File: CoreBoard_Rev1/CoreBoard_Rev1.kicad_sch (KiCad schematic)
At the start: 87 parts, among them J1 RJ45_LED_Shielded, SW1 SW_Push, SW10 SW_Push, SW11 SW_Push, SW12 SW_Push, SW13 SW_Push, SW14 SW_Push, SW15 SW_Push, SW16 SW_SPDT, SW17 SW_SPDT, SW2 SW_Push, SW3 SW_Push, SW4 SW_Push, SW5 SW_Push, SW6 SW_Push, SW7 SW_Push, SW8 SW_Push, SW9 SW_Push, U1 Teensy4.1_DEV-16771, U2 TSR_1-2450, U3 TSR_1-2450, U4 74LS148, U5 74LS148, U6 74LS00

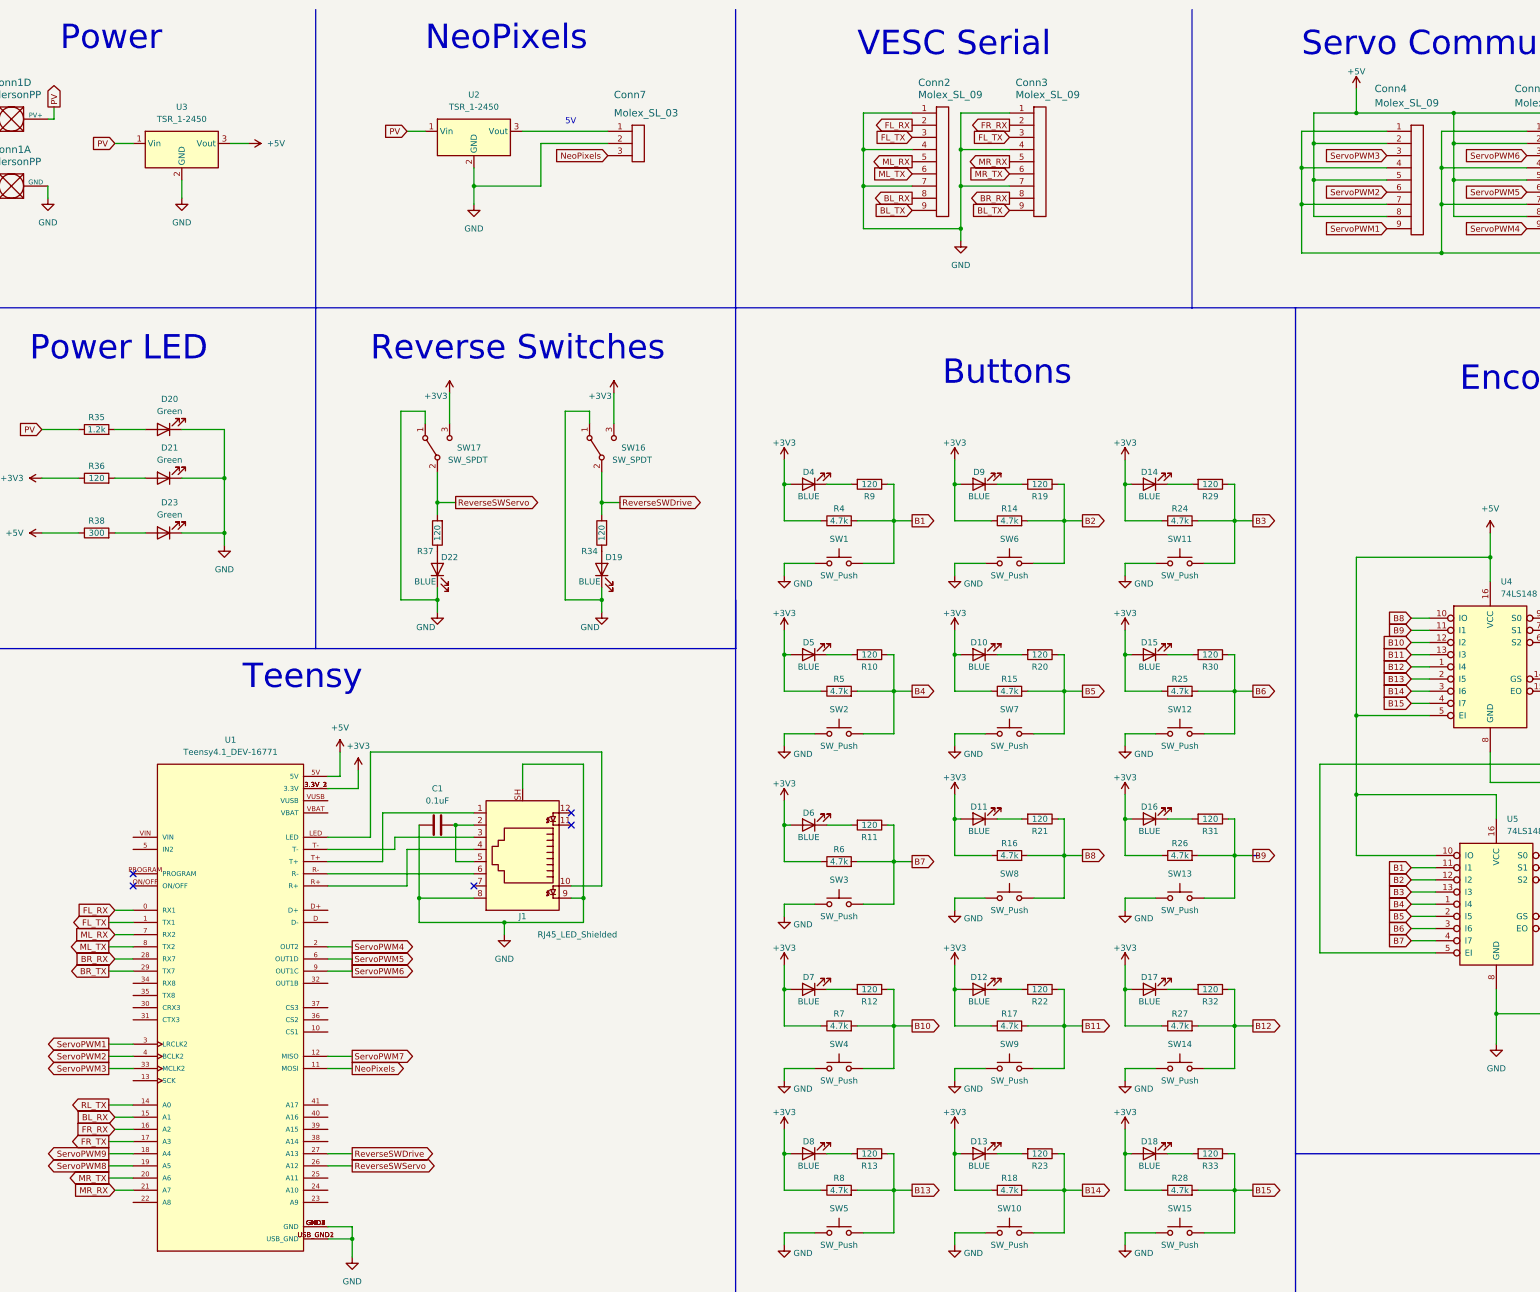
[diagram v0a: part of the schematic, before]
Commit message: Changes to LED Resistance value
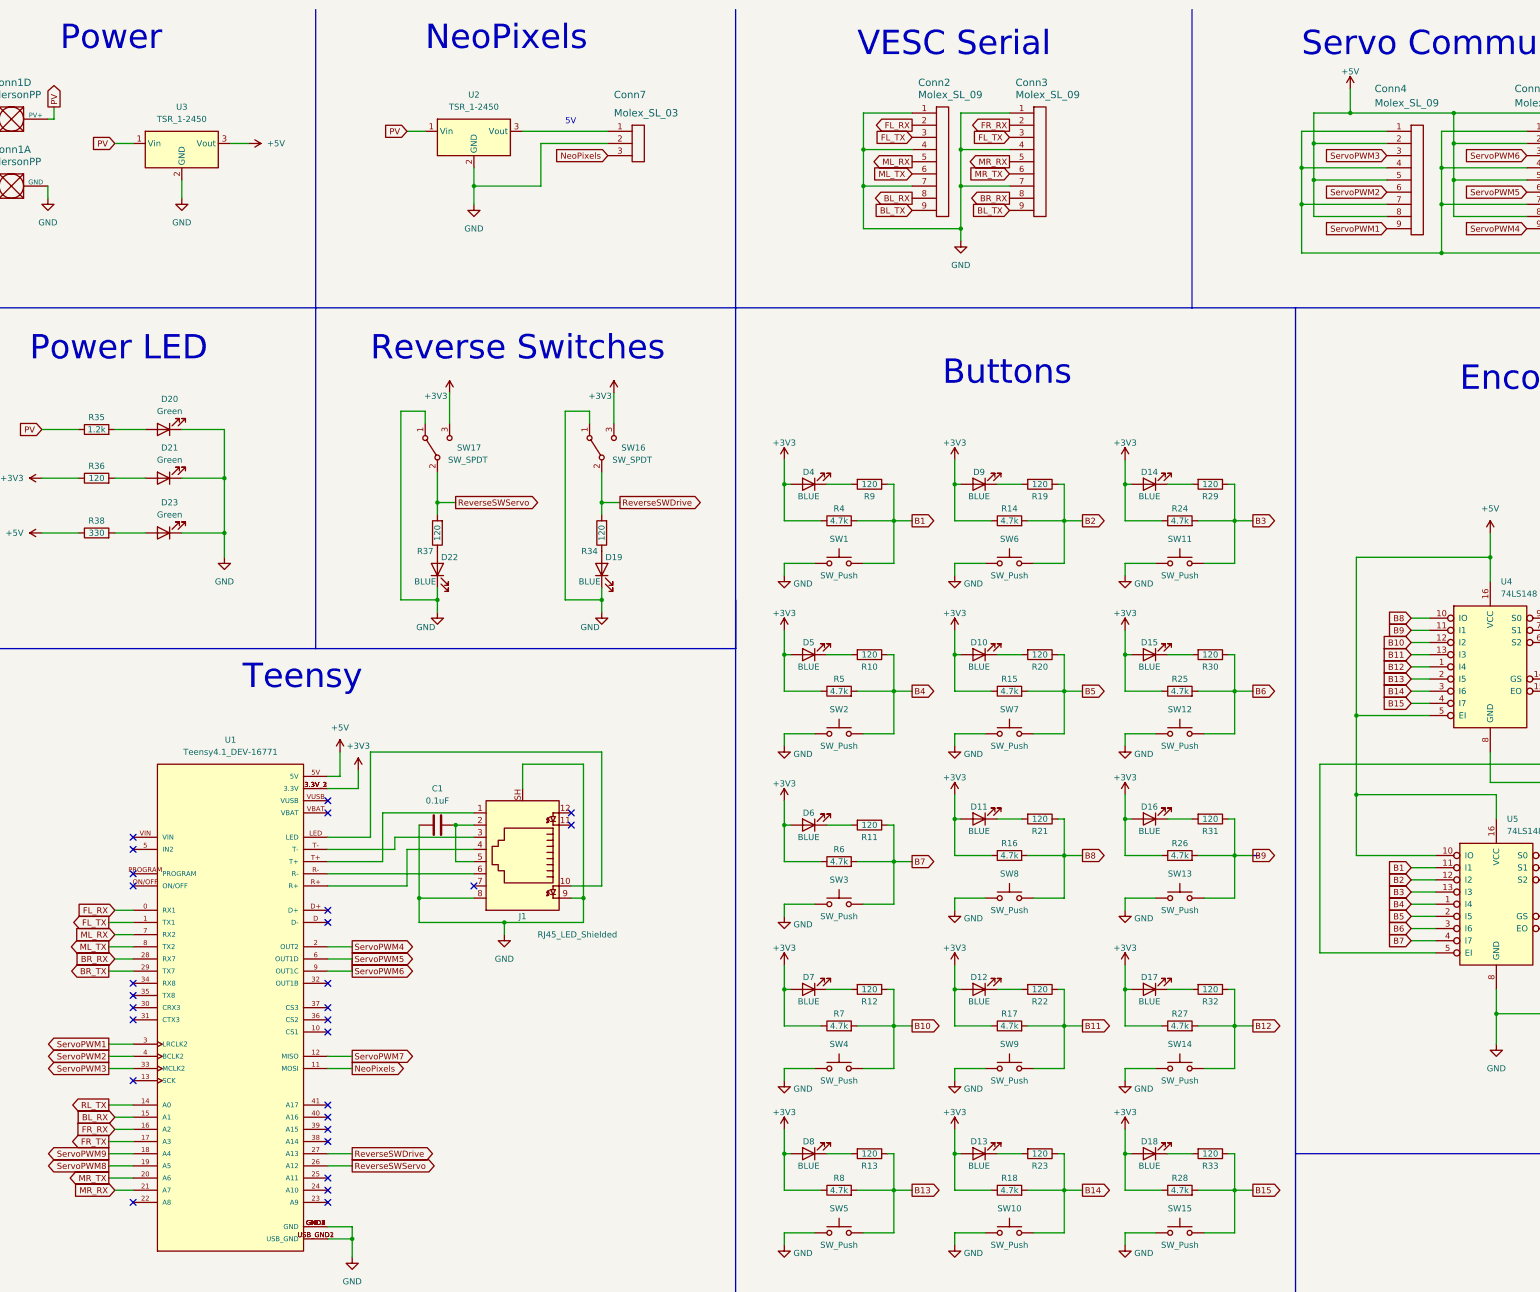
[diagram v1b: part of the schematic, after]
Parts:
- R38: value 300 -> 330
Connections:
- no-connect marks 8 -> 31
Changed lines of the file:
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@@
   (junction (at 326.39 63.5) (diameter 0) (color 0 0 0 0)
   )
-  (junction (at 308.61 34.29) (diameter 0) (color 0 0 0 0)
-  )
   (junction (at 212.09 190.5) (diameter 0) (color 0 0 0 0)
   )
@@
   (junction (at 113.03 198.12) (diameter 0) (color 0 0 0 0)
   )
+  (junction (at 307.34 34.29) (diameter 0) (color 0 0 0 0)
+  )
+  (no_connect (at 53.34 220.98))
+  (no_connect (at 93.98 220.98))
+  (no_connect (at 93.98 248.92))
+  (no_connect (at 93.98 246.38))
+  (no_connect (at 53.34 215.9))
+  (no_connect (at 93.98 177.8))
+  (no_connect (at 53.34 187.96))
+  (no_connect (at 93.98 223.52))
+  (no_connect (at 93.98 203.2))
   (no_connect (at 53.34 195.58))
   (no_connect (at 350.52 204.47))
+  (no_connect (at 93.98 215.9))
+  (no_connect (at 93.98 200.66))
+  (no_connect (at 53.34 218.44))
+  (no_connect (at 93.98 259.08))
   (no_connect (at 144.78 182.88))
+  (no_connect (at 53.34 261.62))
   (no_connect (at 53.34 193.04))
+  (no_connect (at 53.34 185.42))
+  (no_connect (at 93.98 226.06))
+  (no_connect (at 93.98 261.62))
   (no_connect (at 349.25 152.4))
   (no_connect (at 350.52 201.93))
   (no_connect (at 124.46 195.58))
+  (no_connect (at 53.34 223.52))
+  (no_connect (at 93.98 180.34))
+  (no_connect (at 53.34 236.22))
+  (no_connect (at 93.98 241.3))
+  (no_connect (at 93.98 243.84))
   (no_connect (at 144.78 180.34))
+  (no_connect (at 93.98 256.54))
   (wire (pts (xy 260.35 233.68) (xy 266.7 233.68))
     (stroke (width 0) (type default))
   )
+  (wire (pts (xy 307.34 34.29) (xy 328.93 34.29))
+    (stroke (width 0) (type default))
+  )
   (wire (pts (xy 260.35 251.46) (xy 260.35 259.08))
     (stroke (width 0) (type default))
@@
     (stroke (width 0) (type default))
   )
+  (wire (pts (xy 307.34 34.29) (xy 299.72 34.29))
+    (stroke (width 0) (type default))
+  )
   (wire (pts (xy 224.79 217.17) (xy 224.79 224.79))
     (stroke (width 0) (type default))
@@
     (stroke (width 0) (type default))
   )
-  (wire (pts (xy 102.87 167.64) (xy 102.87 185.42))
-    (stroke (width 0) (type default))
-  )
   (wire (pts (xy 48.26 241.3) (xy 53.34 241.3))
     (stroke (width 0) (type default))
@@
     (stroke (width 0) (type default))
   )
-  (wire (pts (xy 102.87 167.64) (xy 151.13 167.64))
-    (stroke (width 0) (type default))
-  )
   (wire (pts (xy 116.84 138.43) (xy 116.84 135.89))
     (stroke (width 0) (type default))
@@
     (stroke (width 0) (type default))
   )
-  (wire (pts (xy 299.72 34.29) (xy 308.61 34.29))
-    (stroke (width 0) (type default))
-  )
   (wire (pts (xy 260.35 270.51) (xy 260.35 267.97))
     (stroke (width 0) (type default))
@@
     (stroke (width 0) (type default))
   )
-  (wire (pts (xy 308.61 34.29) (xy 328.93 34.29))
-    (stroke (width 0) (type default))
-  )
   (wire (pts (xy 247.65 163.83) (xy 247.65 154.94))
     (stroke (width 0) (type default))
@@
     (stroke (width 0) (type default))
   )
-  (wire (pts (xy 72.39 121.92) (xy 72.39 124.46))
+  (wire (pts (xy 72.39 121.92) (xy 72.39 127))
     (stroke (width 0) (type default))
   )
@@
     (stroke (width 0) (type default))
   )
+  (wire (pts (xy 102.87 167.64) (xy 102.87 185.42))
+    (stroke (width 0) (type default))
+  )
+  (wire (pts (xy 151.13 167.64) (xy 102.87 167.64))
+    (stroke (width 0) (type default))
+  )
   (wire (pts (xy 247.65 259.08) (xy 251.46 259.08))
     (stroke (width 0) (type default))
@@
     (stroke (width 0) (type default))
   )
-  (wire (pts (xy 308.61 29.21) (xy 308.61 34.29))
+  (wire (pts (xy 307.34 29.21) (xy 307.34 34.29))
     (stroke (width 0) (type default))
   )
@@
       (effects (font (size 1.27 1.27)))
     )
-    (property "Value" "300" (at 45.72 121.92 90)
+    (property "Value" "330" (at 45.72 121.92 90)
       (effects (font (size 1.27 1.27)))
     )
@@
     )
   )
-  (symbol (lib_id "power:GND") (at 72.39 124.46 0) (unit 1)
+  (symbol (lib_id "power:GND") (at 72.39 127 0) (unit 1)
     (in_bom yes) (on_board yes) (dnp no) (fields_autoplaced)
-    (property "Reference" "#PWR047" (at 72.39 130.81 0)
+    (property "Reference" "#PWR047" (at 72.39 133.35 0)
       (effects (font (size 1.27 1.27)) hide)
     )
-    (property "Value" "GND" (at 72.39 129.54 0)
+    (property "Value" "GND" (at 72.39 132.08 0)
       (effects (font (size 1.27 1.27)))
     )
-    (property "Footprint" "" (at 72.39 124.46 0)
+    (property "Footprint" "" (at 72.39 127 0)
       (effects (font (size 1.27 1.27)) hide)
     )
-    (property "Datasheet" "" (at 72.39 124.46 0)
+    (property "Datasheet" "" (at 72.39 127 0)
       (effects (font (size 1.27 1.27)) hide)
     )
@@
     )
   )
-  (symbol (lib_id "power:+5V") (at 308.61 29.21 0) (unit 1)
+  (symbol (lib_id "power:+5V") (at 307.34 29.21 0) (unit 1)
     (in_bom yes) (on_board yes) (dnp no) (fields_autoplaced)
-    (property "Reference" "#PWR045" (at 308.61 33.02 0)
+    (property "Reference" "#PWR045" (at 307.34 33.02 0)
       (effects (font (size 1.27 1.27)) hide)
     )
-    (property "Value" "+5V" (at 308.61 25.6342 0)
+    (property "Value" "+5V" (at 307.34 25.6342 0)
       (effects (font (size 1.27 1.27)))
     )
-    (property "Footprint" "" (at 308.61 29.21 0)
+    (property "Footprint" "" (at 307.34 29.21 0)
       (effects (font (size 1.27 1.27)) hide)
     )
-    (property "Datasheet" "" (at 308.61 29.21 0)
+    (property "Datasheet" "" (at 307.34 29.21 0)
       (effects (font (size 1.27 1.27)) hide)
     )

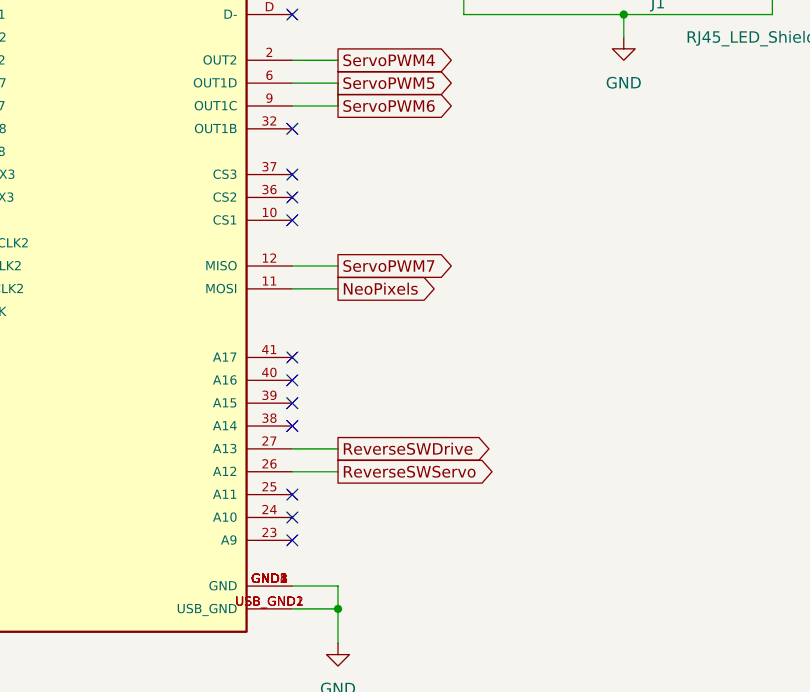
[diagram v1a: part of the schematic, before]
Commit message: Encoder Outputs in Teensy, Reverse Input
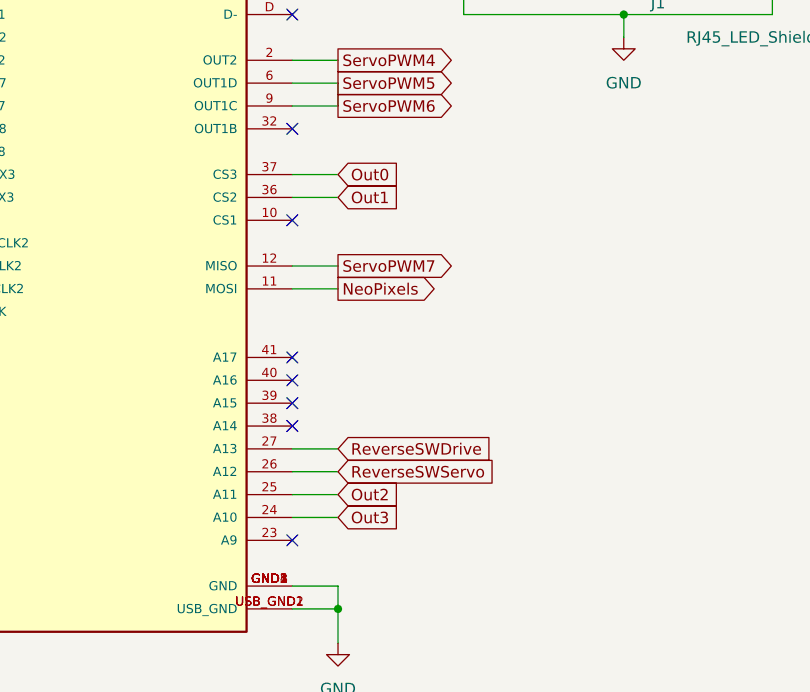
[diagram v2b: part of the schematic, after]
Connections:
- net Out0: now also U1.37 (CS3)
- net Out1: now also U1.36 (CS2)
- net Out2: now also U1.25 (A11)
- net Out3: now also U1.24 (A10)
- no-connect marks 31 -> 27
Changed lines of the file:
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@@
   )
   (no_connect (at 53.34 220.98))
-  (no_connect (at 93.98 220.98))
   (no_connect (at 93.98 248.92))
   (no_connect (at 93.98 246.38))
@@
   (no_connect (at 93.98 177.8))
   (no_connect (at 53.34 187.96))
-  (no_connect (at 93.98 223.52))
   (no_connect (at 93.98 203.2))
   (no_connect (at 53.34 195.58))
@@
   (no_connect (at 93.98 200.66))
   (no_connect (at 53.34 218.44))
-  (no_connect (at 93.98 259.08))
   (no_connect (at 144.78 182.88))
   (no_connect (at 53.34 261.62))
@@
   (no_connect (at 93.98 243.84))
   (no_connect (at 144.78 180.34))
-  (no_connect (at 93.98 256.54))
   (wire (pts (xy 260.35 233.68) (xy 266.7 233.68))
     (stroke (width 0) (type default))
@@
     (stroke (width 0) (type default))
   )
+  (wire (pts (xy 93.98 223.52) (xy 99.06 223.52))
+    (stroke (width 0) (type default))
+  )
   (wire (pts (xy 109.22 96.52) (xy 114.3 96.52))
     (stroke (width 0) (type default))
@@
     (stroke (width 0) (type default))
   )
+  (wire (pts (xy 93.98 256.54) (xy 99.06 256.54))
+    (stroke (width 0) (type default))
+  )
   (wire (pts (xy 48.26 208.28) (xy 53.34 208.28))
     (stroke (width 0) (type default))
@@
     (stroke (width 0) (type default))
   )
+  (wire (pts (xy 93.98 220.98) (xy 99.06 220.98))
+    (stroke (width 0) (type default))
+  )
   (wire (pts (xy 151.13 115.57) (xy 151.13 118.11))
     (stroke (width 0) (type default))
@@
   )
   (wire (pts (xy 260.35 163.83) (xy 266.7 163.83))
+    (stroke (width 0) (type default))
+  )
+  (wire (pts (xy 93.98 259.08) (xy 99.06 259.08))
     (stroke (width 0) (type default))
   )
@@
     )
   )
+  (global_label "Out2" (shape input) (at 99.06 256.54 0) (fields_autoplaced)
+    (effects (font (size 1.27 1.27)) (justify left))
+    (property "Intersheetrefs" "${INTERSHEET_REFS}" (at 106.4599 256.54 0)
+      (effects (font (size 1.27 1.27)) (justify left) hide)
+    )
+  )
   (global_label "B11" (shape output) (at 251.46 224.79 0) (fields_autoplaced)
     (effects (font (size 1.27 1.27)) (justify left))
@@
     )
   )
-  (global_label "ReverseSWDrive" (shape output) (at 99.06 251.46 0) (fields_autoplaced)
+  (global_label "Out0" (shape input) (at 99.06 220.98 0) (fields_autoplaced)
+    (effects (font (size 1.27 1.27)) (justify left))
+    (property "Intersheetrefs" "${INTERSHEET_REFS}" (at 106.4599 220.98 0)
+      (effects (font (size 1.27 1.27)) (justify left) hide)
+    )
+  )
+  (global_label "ReverseSWDrive" (shape input) (at 99.06 251.46 0) (fields_autoplaced)
     (effects (font (size 1.27 1.27)) (justify left))
     (property "Intersheetrefs" "${INTERSHEET_REFS}" (at 116.741 251.46 0)
@@
     )
   )
-  (global_label "ReverseSWServo" (shape output) (at 99.06 254 0) (fields_autoplaced)
+  (global_label "ReverseSWServo" (shape input) (at 99.06 254 0) (fields_autoplaced)
     (effects (font (size 1.27 1.27)) (justify left))
     (property "Intersheetrefs" "${INTERSHEET_REFS}" (at 117.2247 254 0)
@@
     )
   )
+  (global_label "Out3" (shape input) (at 99.06 259.08 0) (fields_autoplaced)
+    (effects (font (size 1.27 1.27)) (justify left))
+    (property "Intersheetrefs" "${INTERSHEET_REFS}" (at 106.4599 259.08 0)
+      (effects (font (size 1.27 1.27)) (justify left) hide)
+    )
+  )
   (global_label "MR_TX" (shape output) (at 48.26 256.54 180) (fields_autoplaced)
     (effects (font (size 1.27 1.27)) (justify right))
@@
     )
   )
+  (global_label "Out1" (shape input) (at 99.06 223.52 0) (fields_autoplaced)
+    (effects (font (size 1.27 1.27)) (justify left))
+    (property "Intersheetrefs" "${INTERSHEET_REFS}" (at 106.4599 223.52 0)
+      (effects (font (size 1.27 1.27)) (justify left) hide)
+    )
+  )

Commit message: Review Fixes
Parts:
- removed D22: BLUE, LED_SMD:LED_0603_1608Metric_Pad1.05x0.95mm_HandSolder, symbol Device:LED
- removed R37: 120, Resistor_SMD:R_0603_1608Metric_Pad0.98x0.95mm_HandSolder, symbol Device:R
- removed SW17: SW_SPDT, Button_Switch_THT:SW_Slide_1P2T_CK_OS102011MS2Q, symbol Switch:SW_SPDT
- removed U6: 74LS00, Package_SO:SO-14_5.3x10.2mm_P1.27mm, symbol 74xx:74LS00
- added U6: 74HC00, symbol 74xx:74HC00
- R10, R11, R12, R13, R19, R20, R21, R22, R23, R29, R30, R31, R32, R33, R34, R36, R9: value 120 -> 100
- R35: value 1.2k -> 3k
- R38: value 330 -> 300
- U4, U5: value 74LS148 -> 74HC148
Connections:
- net +3V3: now also U4.16 (VCC), U4.5 (EI), U5.10 (IO), U5.16 (VCC), U6.14 (VCC)
- net +5V: now also U1.VIN; no longer U1.5V, U4.16 (VCC), U4.5 (EI), U5.10 (IO), U5.16 (VCC)
- net GND: now also U6.7 (GND)
- net Out0: now also U6.3
- net Out1: now also U6.6
- net Out2: now also U6.8
- net at U4.9 (S0): now also U6.1
- net at U5.9 (S0): now also U6.2
- net at U4.6 (S2): now also U6.9
- net at U5.6 (S2): now also U6.10
- net at U4.7 (S1): now also U6.4
- net at U5.7 (S1): now also U6.5
- net ReverseSWDrive renamed ReverseSW
- net ReverseSWServo: no longer names the net of U1.26 (A12)
- no-connect marks 27 -> 28
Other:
- moved on the sheet: Conn3, D19, R34, SW16
